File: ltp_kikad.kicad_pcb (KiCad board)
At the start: 2 copper layers, 65 x 56.5 mm, 22 parts, among them IC1 SamacSys_Parts_HT16K33-28SOP, IC2 SamacSys_Parts_HT16K33-28SOP, J2 RPi_GPIO

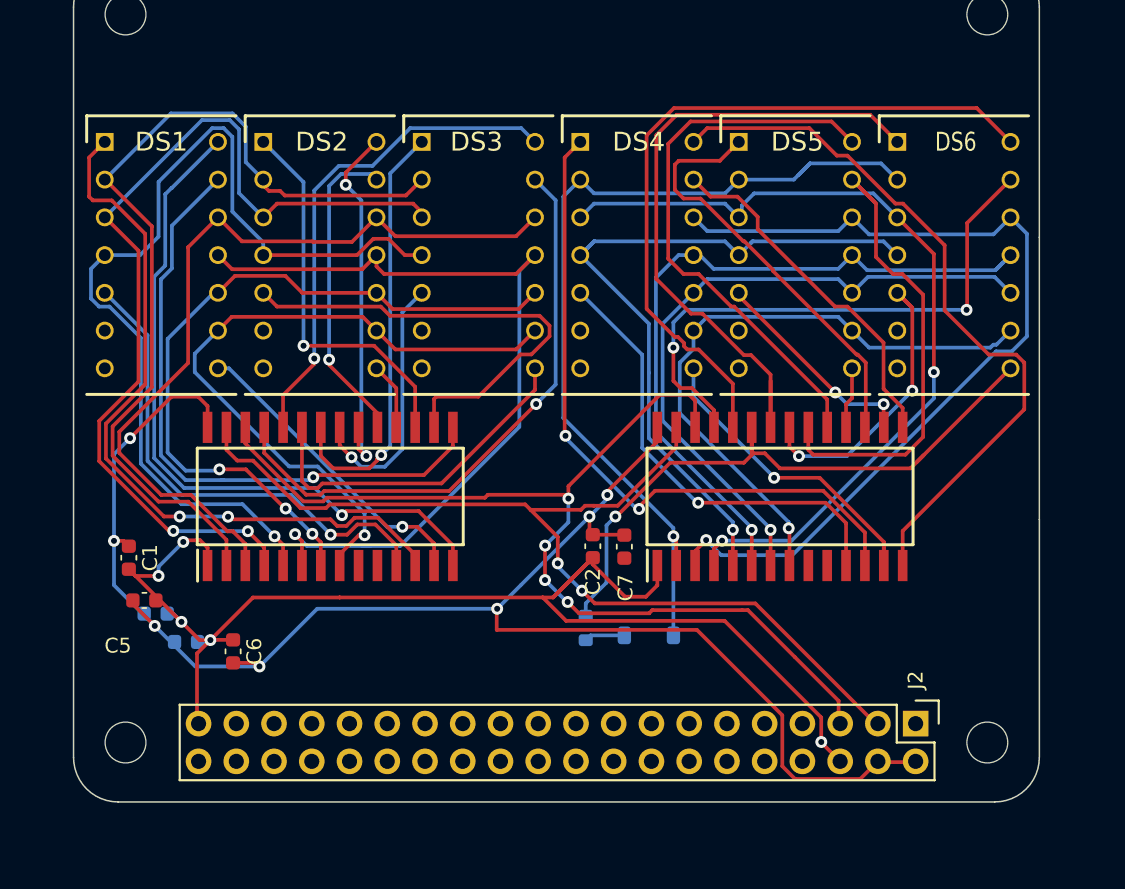
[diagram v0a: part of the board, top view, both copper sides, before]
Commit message: Add qwiic stemma i2c connector
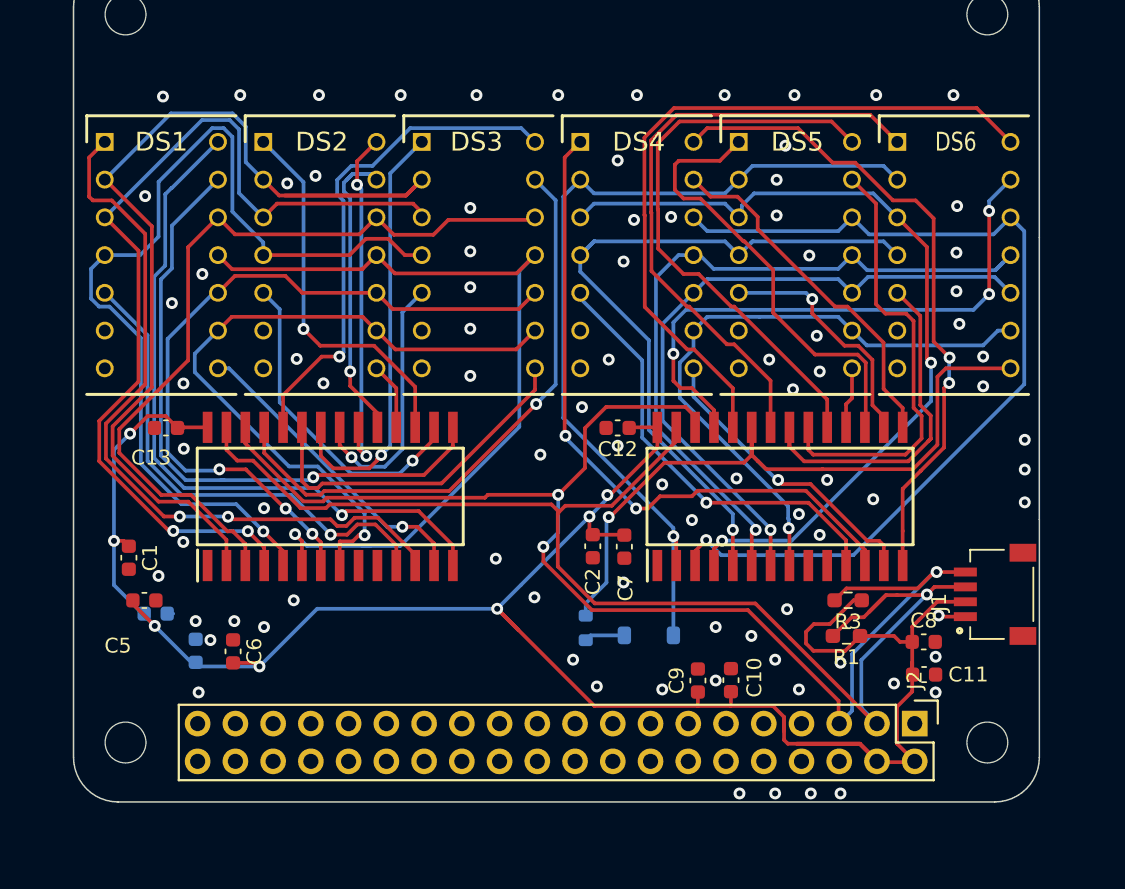
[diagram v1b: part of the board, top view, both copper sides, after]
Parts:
- added C10: 10uF, Capacitor_SMD:C_0603_1608Metric, F.Cu at (163.2, 101.4)
- added C11: 10uF, Capacitor_SMD:C_0603_1608Metric, F.Cu at (176.2, 101.0)
- added C12: 10uF, Capacitor_SMD:C_0603_1608Metric, F.Cu at (155.6, 84.4)
- added C13: 10uF, Capacitor_SMD:C_0603_1608Metric, F.Cu at (125.2, 84.4)
- added C8: 10uF, Capacitor_SMD:C_0603_1608Metric, F.Cu at (176.2, 98.8)
- added C9: 10uF, Capacitor_SMD:C_0603_1608Metric, F.Cu at (161.0, 101.4)
- added J1: SM04B-SRSS-TB(LF)(SN), LTP-305G:JST_SM04B-SRSS-TB(LF)(SN), F.Cu at (179.0, 95.6)
- added R1: DNP, Resistor_SMD:R_0603_1608Metric_Pad0.98x0.95mm_HandSolder, F.Cu at (171.0, 98.4)
- added R3: DNP, Resistor_SMD:R_0603_1608Metric_Pad0.98x0.95mm_HandSolder, F.Cu at (171.1, 96.0)
- moved C4 0.88 mm to (127.2, 99.4), turned to -90 degrees
- moved J2 0.06 mm to (151.4, 105.6)
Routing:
- net GND: track 90.1 -> 2.43 mm, vias 5 -> 87
- net +5V: track 109.8 -> 146.3 mm
- net SDA: track 67.2 -> 89.0 mm, vias 2 -> 1
- net SCL: track 69.6 -> 91.2 mm, vias 4 -> 3
- net an9: track 32.3 -> 21.9 mm, vias 0 -> 1
- net ca0: track 59.9 -> 69.7 mm
- net 2_an11: track 48.8 -> 44.2 mm, vias 0 -> 2
- net 2_an4: track 20.0 -> 24.1 mm, vias 2 -> 0
- net 2_an2: track 43.2 -> 47.3 mm
- net 2_an3: track 43.2 -> 41.1 mm
- net 2_an9: track 14.5 -> 16.5 mm, vias 2 -> 1
- net 2_an5: track 31.7 -> 29.9 mm
- net 2_an12: track 22.0 -> 20.2 mm
- net 2_an8: track 28.7 -> 30.4 mm
- net 2_ca1: track 61.6 -> 63.3 mm
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
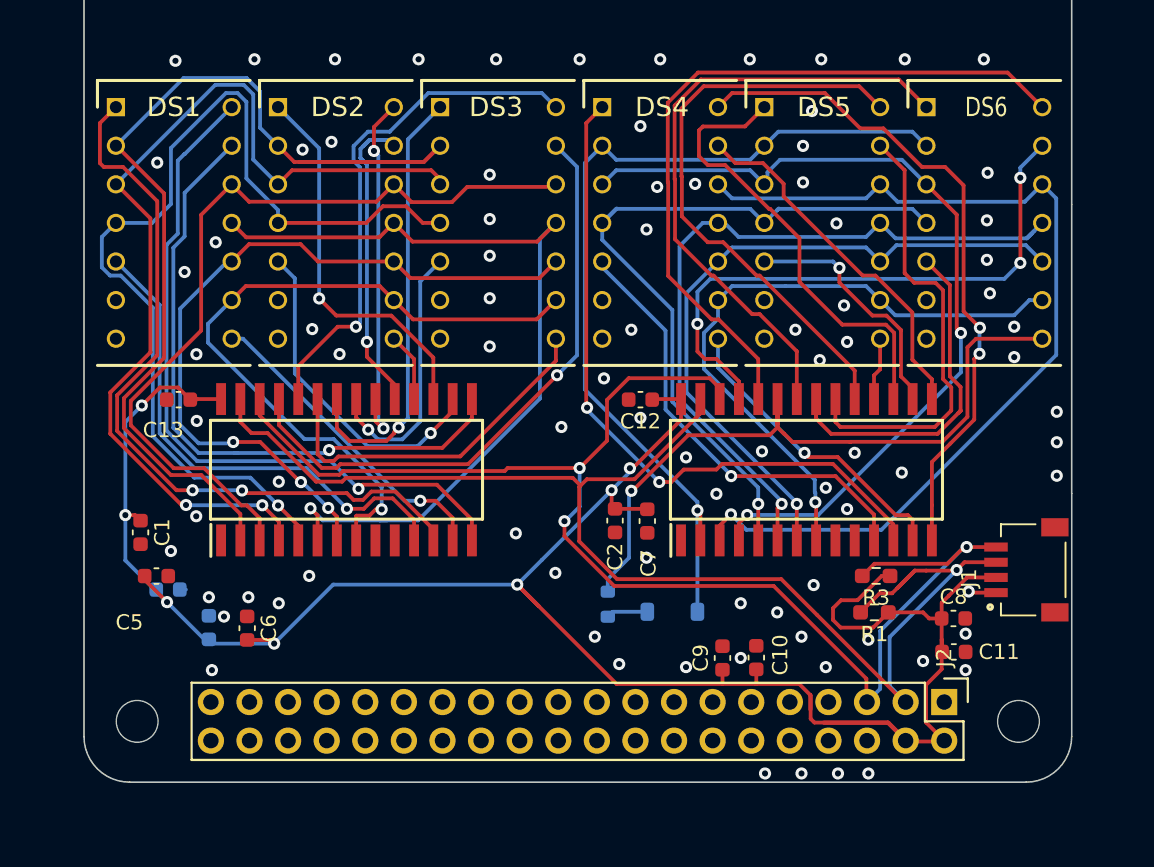
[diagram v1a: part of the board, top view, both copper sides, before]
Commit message: Optimize design, add bypass caps
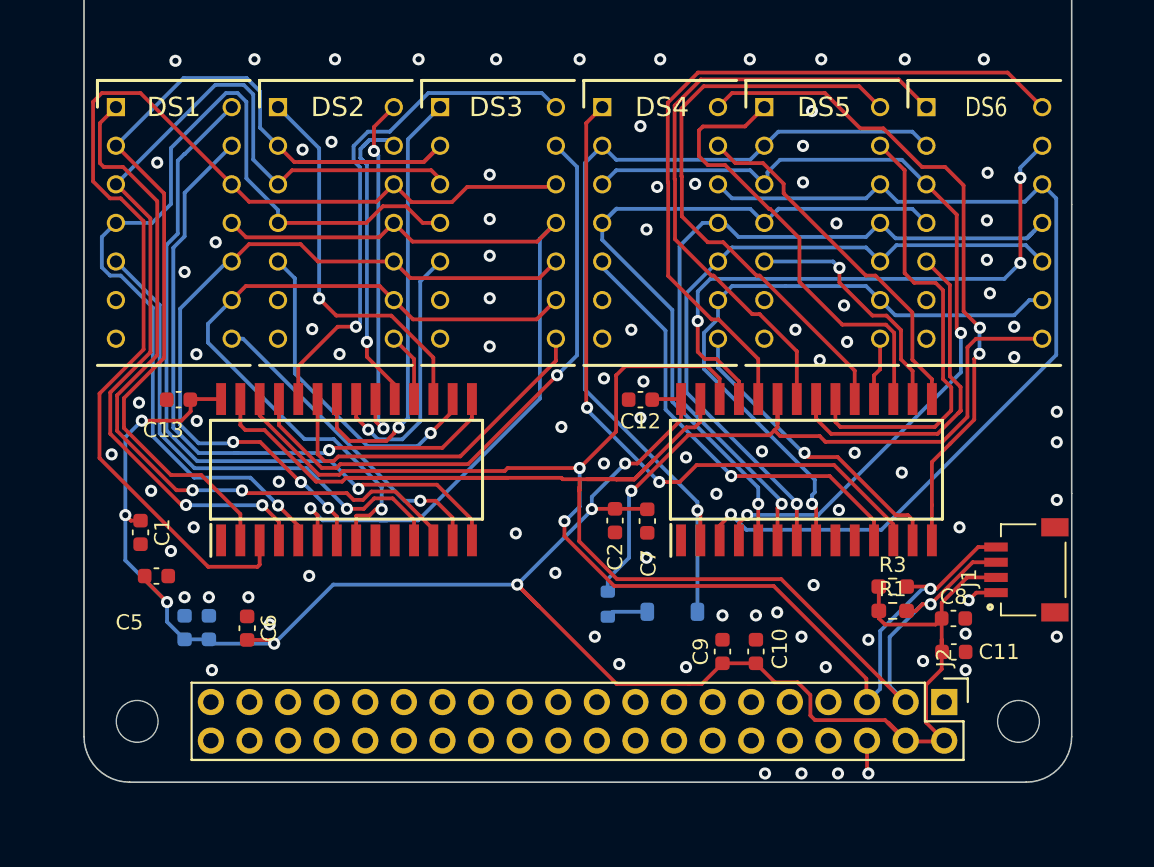
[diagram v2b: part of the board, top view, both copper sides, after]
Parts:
- moved C3 2.73 mm to (125.6, 99.4), turned to -90 degrees
- moved R3 1.29 mm to (172.2, 96.7), turned to 0 degrees
- moved R1 1.20 mm to (172.2, 98.3), turned to 0 degrees
- moved C9 0.43 mm to (161.0, 101.0)
- moved C10 0.40 mm to (163.2, 101.0)
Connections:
- J1 pad S1: unconnected-(J1-SHIELD-PadS1) -> GND
- J1 pad S2: unconnected-(J1-SHIELD-PadS1) -> GND
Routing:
- net ca1: track 54.3 -> 76.7 mm
- net +5V: track 146.3 -> 135.8 mm
- net SDA: track 89.0 -> 98.7 mm
- net SCL: track 91.2 -> 86.9 mm
- net GND: track 2.43 -> 4.20 mm, vias 87 -> 93
- net 2_an2: track 47.3 -> 45.5 mm

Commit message: Minor fixes
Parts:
- added C14: 10uF, Capacitor_SMD:C_0603_1608Metric, B.Cu at (153.8, 89.4)
- added C15: 10uF, Capacitor_SMD:C_0603_1608Metric, B.Cu at (149.4, 95.4)
- moved R2 5.45 mm to (153.8, 92.4)
- moved D1 5.16 mm to (157.5, 93.2)
- moved C1 2.07 mm to (123.6, 95.0), turned to 0 degrees
- moved C5 1.00 mm to (123.6, 97.0)
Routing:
- net SDA: track 98.7 -> 82.6 mm
- net +5V: track 135.8 -> 129.8 mm, vias 7 -> 6
- net ca0: track 69.7 -> 63.8 mm
- net 2_an2: track 45.5 -> 40.2 mm
- net 2_ca0: track 59.1 -> 54.0 mm
- net SCL: track 86.9 -> 89.5 mm
- net an13: track 49.8 -> 51.6 mm
- net ca2: track 63.6 -> 65.3 mm
- net ca1: track 76.7 -> 75.1 mm
- net ca3: track 64.1 -> 63.1 mm
- net Net-(D1-K): track 2.73 -> 2.12 mm
- net GND: vias 93 -> 94

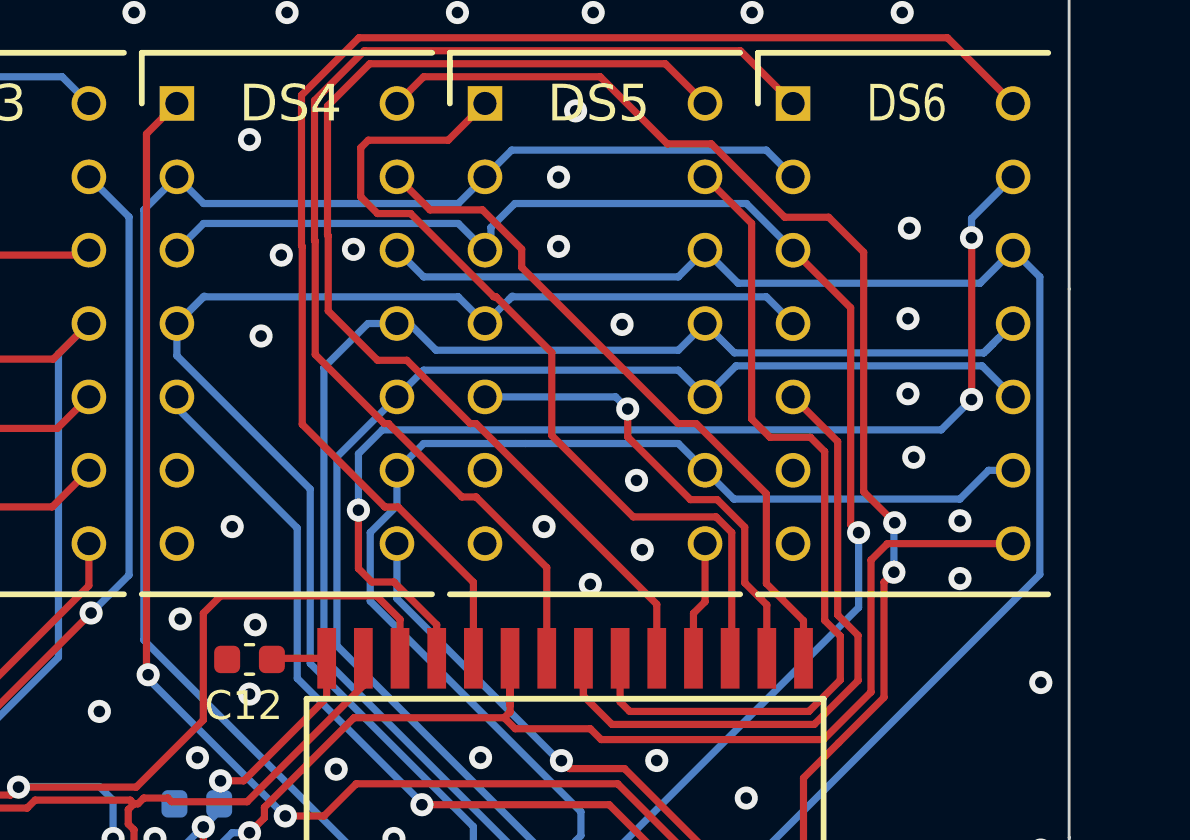
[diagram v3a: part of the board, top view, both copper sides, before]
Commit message: Optimize filled zones
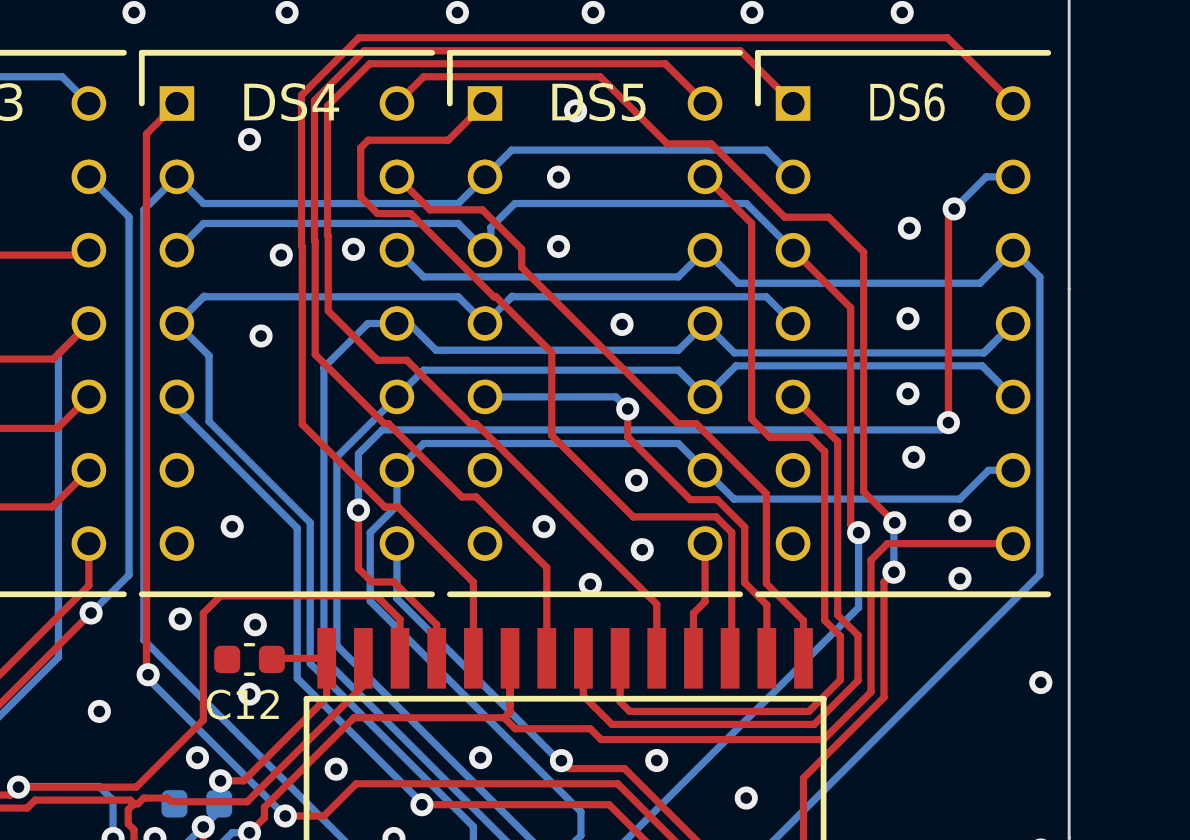
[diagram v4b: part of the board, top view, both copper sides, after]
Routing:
- net 2_an0: track 39.0 -> 39.5 mm
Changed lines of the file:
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@@
   (via (at 163.3389 91.2611) (size 0.8) (drill 0.4) (layers "F.Cu" "B.Cu") (net 10))
   (segment (start 153.0719 72.7686) (end 153.9969 71.8436) (width 0.25) (layer "B.Cu") (net 10))
+  (segment (start 157.6889 79.665504) (end 154.187 76.163604) (width 0.25) (layer "B.Cu") (net 10))
+  (segment (start 164.5654 71.9431) (end 163.7399 72.7686) (width 0.25) (layer "B.Cu") (net 10))
   (segment (start 163.3389 91.2611) (end 163.3389 90.188296) (width 0.25) (layer "B.Cu") (net 10))
-  (segment (start 164.5654 71.9431) (end 163.7399 72.7686) (width 0.25) (layer "B.Cu") (net 10))
+  (segment (start 163.3389 90.188296) (end 157.6889 84.538296) (width 0.25) (layer "B.Cu") (net 10))
   (segment (start 153.9969 71.8436) (end 162.8149 71.8436) (width 0.25) (layer "B.Cu") (net 10))
   (segment (start 164.6649 71.8436) (end 164.5654 71.9431) (width 0.25) (layer "B.Cu") (net 10))
-  (segment (start 157.6889 84.538296) (end 157.6889 78.5019) (width 0.25) (layer "B.Cu") (net 10))
+  (segment (start 154.187 73.8837) (end 153.0719 72.7686) (width 0.25) (layer "B.Cu") (net 10))
+  (segment (start 157.6889 84.538296) (end 157.6889 79.665504) (width 0.25) (layer "B.Cu") (net 10))
+  (segment (start 154.187 76.163604) (end 154.187 73.8837) (width 0.25) (layer "B.Cu") (net 10))
   (segment (start 174.4079 72.7686) (end 173.4829 71.8436) (width 0.25) (layer "B.Cu") (net 10))
   (segment (start 162.8149 71.8436) (end 163.7399 72.7686) (width 0.25) (layer "B.Cu") (net 10))
-  (segment (start 163.3389 90.188296) (end 157.6889 84.538296) (width 0.25) (layer "B.Cu") (net 10))
   (segment (start 173.4829 71.8436) (end 164.6649 71.8436) (width 0.25) (layer "B.Cu") (net 10))
-  (segment (start 153.0719 73.8849) (end 153.0719 72.7686) (width 0.25) (layer "B.Cu") (net 10))
   (segment (start 164.6919 71.8166) (end 164.5654 71.9431) (width 0.25) (layer "B.Cu") (net 10))
-  (segment (start 157.6889 78.5019) (end 153.0719 73.8849) (width 0.25) (layer "B.Cu") (net 10))
   (segment (start 154.0239 71.8166) (end 153.0719 72.7686) (width 0.25) (layer "B.Cu") (net 10))
   (segment (start 170.9589 93.6616) (end 170.9589 92.346595) (width 0.25) (layer "F.Cu") (net 11))
@@
   (segment (start 159.357701 79.229299) (end 159.357701 81.252701) (width 0.25) (layer "F.Cu") (net 31))
   (segment (start 159.357701 81.252701) (end 159.824 81.719) (width 0.25) (layer "F.Cu") (net 31))
-  (segment (start 180.594 75.393) (end 180.594 70) (width 0.25) (layer "F.Cu") (net 31))
+  (segment (start 179.987 68.8) (end 179.787 69) (width 0.25) (layer "F.Cu") (net 31))
   (segment (start 160.587396 81.719) (end 162.0689 83.200504) (width 0.25) (layer "F.Cu") (net 31))
-  (segment (start 180.594 70) (end 180.594 69.807) (width 0.25) (layer "F.Cu") (net 31))
-  (segment (start 180.587 75.4) (end 180.594 75.393) (width 0.25) (layer "F.Cu") (net 31))
-  (segment (start 180.594 69.807) (end 180.587 69.8) (width 0.25) (layer "F.Cu") (net 31))
-  (via (at 180.587 69.8) (size 0.8) (drill 0.4) (layers "F.Cu" "B.Cu") (net 31))
+  (segment (start 179.787 69) (end 179.787 76.2) (width 0.25) (layer "F.Cu") (net 31))
+  (via (at 179.987 68.8) (size 0.8) (drill 0.4) (layers "F.Cu" "B.Cu") (net 31))
   (via (at 159.357701 79.229299) (size 0.8) (drill 0.4) (layers "F.Cu" "B.Cu") (net 31))
-  (via (at 180.587 75.4) (size 0.8) (drill 0.4) (layers "F.Cu" "B.Cu") (net 31))
-  (segment (start 180.587 69.8) (end 180.587 69.1319) (width 0.25) (layer "B.Cu") (net 31))
-  (segment (start 180.587 69.1319) (end 182.0279 67.691) (width 0.25) (layer "B.Cu") (net 31))
-  (segment (start 159.357701 77.279195) (end 160.185296 76.4516) (width 0.25) (layer "B.Cu") (net 31))
-  (segment (start 179.5354 76.4516) (end 180.587 75.4) (width 0.25) (layer "B.Cu") (net 31))
-  (segment (start 160.185296 76.4516) (end 179.5354 76.4516) (width 0.25) (layer "B.Cu") (net 31))
-  (segment (start 159.357701 79.229299) (end 159.357701 77.279195) (width 0.25) (layer "B.Cu") (net 31))
+  (via (at 179.787 76.2) (size 0.8) (drill 0.4) (layers "F.Cu" "B.Cu") (net 31))
+  (segment (start 160.185296 76.4516) (end 159.357701 77.279195) (width 0.25) (layer "B.Cu") (net 31))
+  (segment (start 179.787 76.2) (end 179.5354 76.4516) (width 0.25) (layer "B.Cu") (net 31))
+  (segment (start 159.357701 77.279195) (end 159.357701 79.229299) (width 0.25) (layer "B.Cu") (net 31))
+  (segment (start 179.987 68.8) (end 181.096 67.691) (width 0.25) (layer "B.Cu") (net 31))
+  (segment (start 179.5354 76.4516) (end 160.185296 76.4516) (width 0.25) (layer "B.Cu") (net 31))
+  (segment (start 181.096 67.691) (end 182.0279 67.691) (width 0.25) (layer "B.Cu") (net 31))
   (segment (start 157.412 70.099695) (end 157.412 76.259) (width 0.25) (layer "F.Cu") (net 32))
   (segment (start 182.0279 65.1486) (end 179.7529 62.8736) (width 0.25) (layer "F.Cu") (net 32))
